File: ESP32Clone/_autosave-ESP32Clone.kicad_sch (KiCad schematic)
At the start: 34 parts, among them J1 Connector, USB-TYPE-C-16P, U1 TPS54331DR, U2 ESP32-C3FH4, X1 40MHz, 15pF

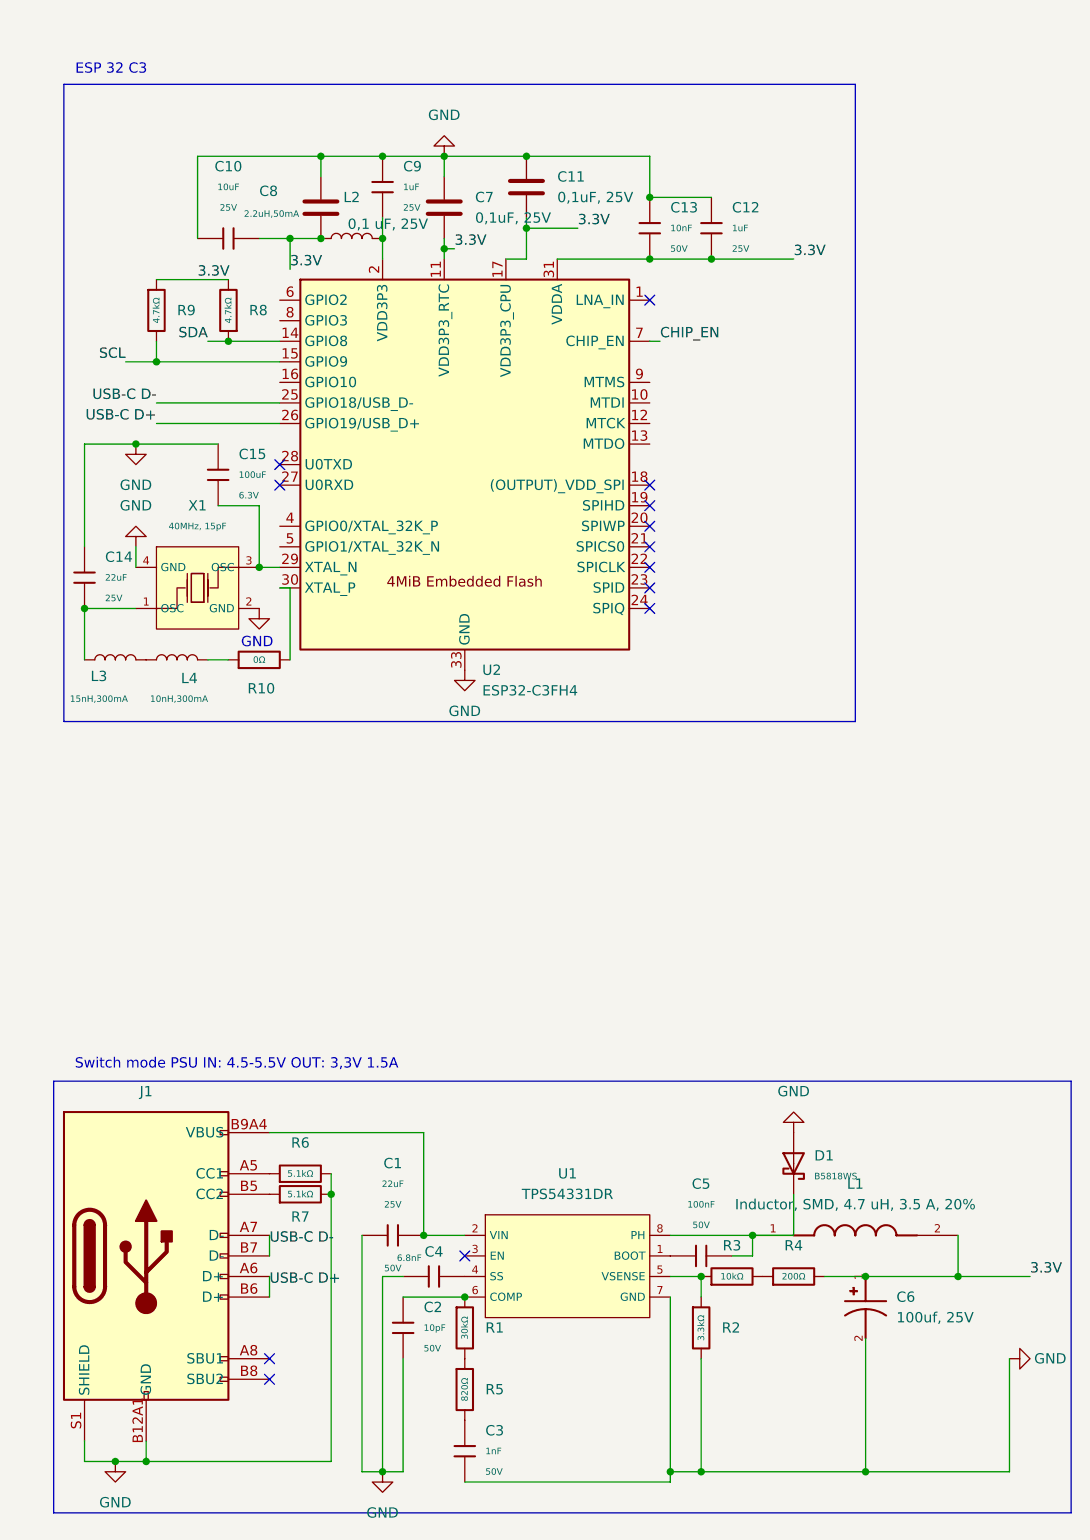
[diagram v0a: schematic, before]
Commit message: Added connecter and reset switch
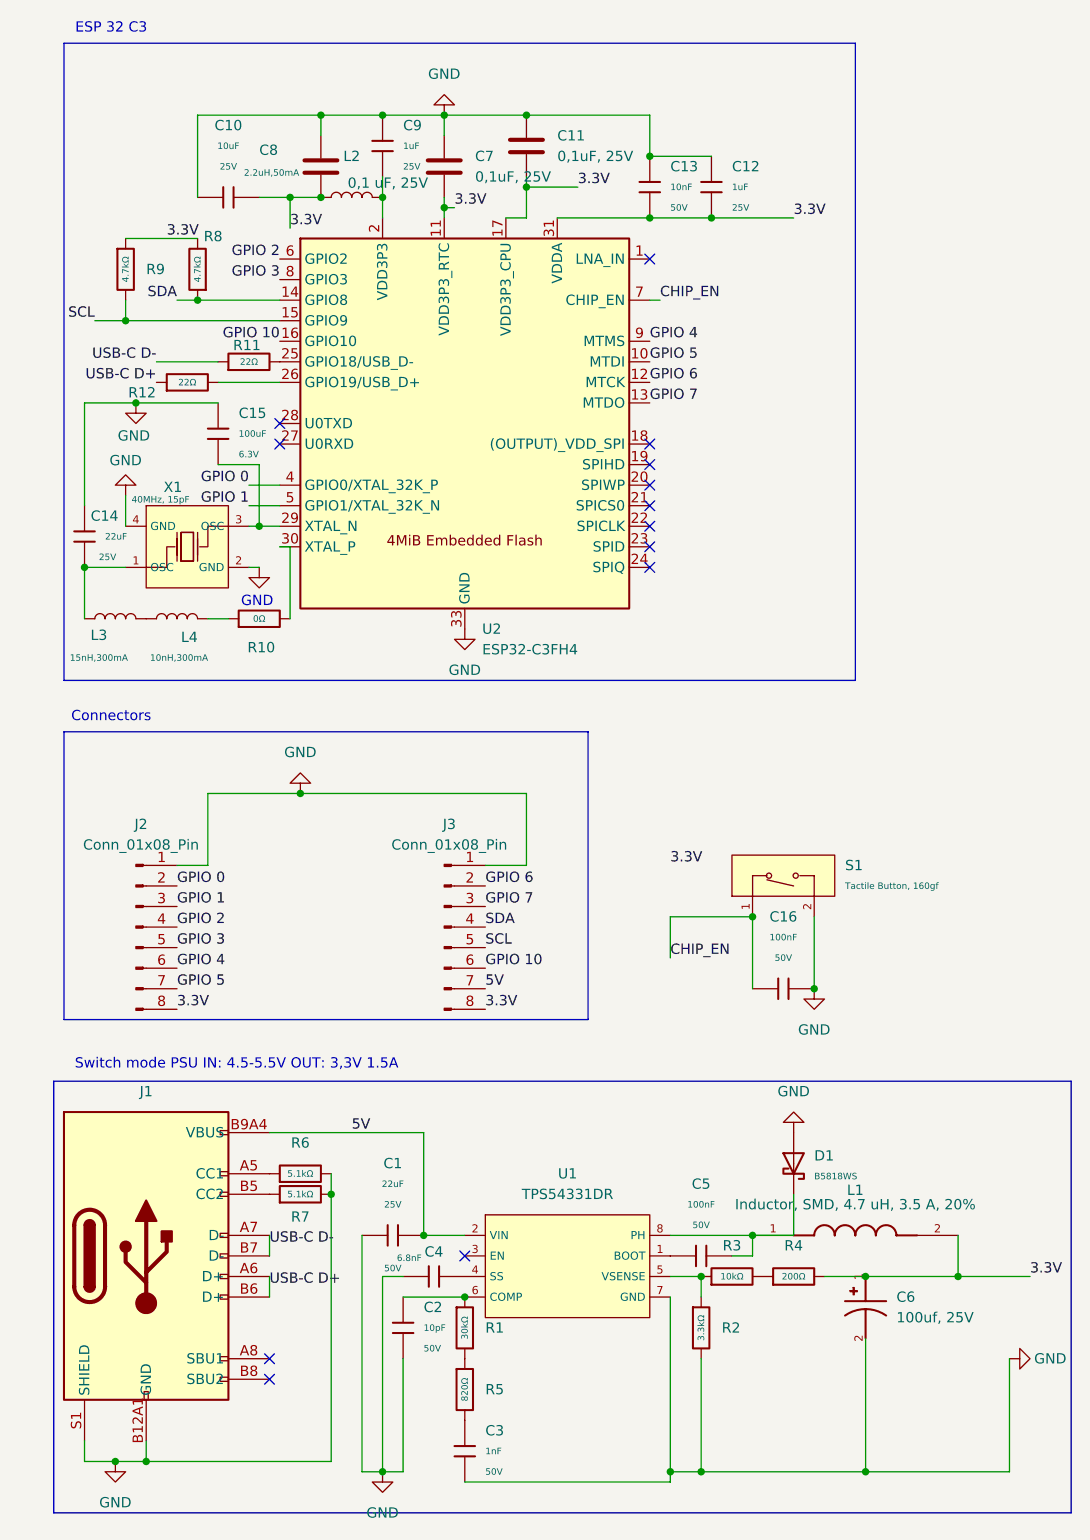
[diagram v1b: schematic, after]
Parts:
- added C16: 100nF, PCM_JLCPCB:C_0603, symbol PCM_JLCPCB-Capacitors:0603,100nF
- added J2, J3: Conn_01x08_Pin, symbol Connector:Conn_01x08_Pin
- added R11, R12: 22Ω, PCM_JLCPCB:R_0805, symbol PCM_JLCPCB-Resistors:0805,22Ω
- added S1: Tactile Button, 160gf, PCM_JLCPCB:SW_TS-1088-AR02016, symbol PCM_JLCPCB-Connectors_Buttons:Tactile Button, 160gf, 12V, 50mA, 4.0mm
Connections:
- net 3.3V: now also J2.8 (Pin_8), J3.8 (Pin_8)
- net CHIP_EN: now also C16.1, S1.1 (A)
- net GND: now also C16.2, J2.1 (Pin_1), J3.1 (Pin_1), S1.2 (B)
- net SCL: now also J3.5 (Pin_5)
- net SDA: now also J3.4 (Pin_4)
- net USB-C D+: now also R12.1; no longer U2.26 (GPIO19/USB_D+)
- net USB-C D-: now also R11.1; no longer U2.25 (GPIO18/USB_D-)
- net 5V: now reaches C1.2, J1.A9B4 (VBUS), J1.B9A4 (VBUS), U1.2 (VIN)
- net 5V: now also J3.7 (Pin_7)
- net GPIO 5: now reaches U2.10 (MTDI)
- net GPIO 5: now also J2.7 (Pin_7)
- net GPIO 6: now reaches U2.12 (MTCK)
- net GPIO 6: now also J3.2 (Pin_2)
- net GPIO 7: now reaches U2.13 (MTDO)
- net GPIO 7: now also J3.3 (Pin_3)
- net GPIO 10: now reaches U2.16 (GPIO10)
- net GPIO 10: now also J3.6 (Pin_6)
- net GPIO 0: now reaches U2.4 (GPIO0/XTAL_32K_P)
- net GPIO 0: now also J2.2 (Pin_2)
- net GPIO 1: now reaches U2.5 (GPIO1/XTAL_32K_N)
- net GPIO 1: now also J2.3 (Pin_3)
- net GPIO 2: now reaches U2.6 (GPIO2)
- net GPIO 2: now also J2.4 (Pin_4)
- net GPIO 3: now reaches U2.8 (GPIO3)
- net GPIO 3: now also J2.5 (Pin_5)
- net GPIO 4: now reaches U2.9 (MTMS)
- net GPIO 4: now also J2.6 (Pin_6)
- new net: R12.2, U2.26 (GPIO19/USB_D+)
- new net: R11.2, U2.25 (GPIO18/USB_D-)
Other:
- note added: "Connectors"
- moved on the sheet: C10, C11, C12, C13, C14, C15, C7, C8, C9, L2, L3, L4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
